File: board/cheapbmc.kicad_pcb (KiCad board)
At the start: 2 copper layers, 57.2 x 46.4 mm, 22 parts, among them J1 Conn_01x02_Male, J2 atxpanel, J3 atxpanel, J4 Conn_01x03_Male, K1 SILxx-1Axx-71x, K2 SILxx-1Axx-71x, Q1 BC547, Q2 BC547, SW1 SW_Push, U1 NodeMCU1.0(ESP-12E)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

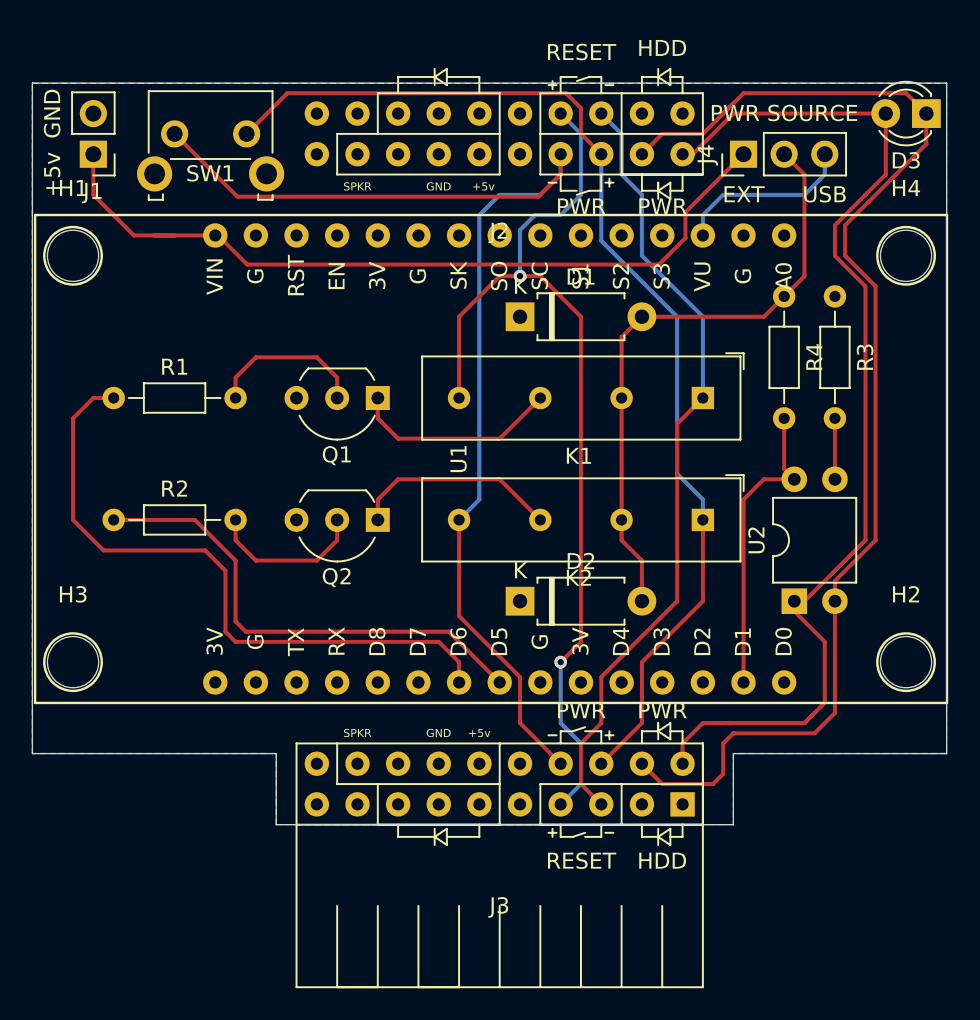
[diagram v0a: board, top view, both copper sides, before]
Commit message: remove text from mounting holes
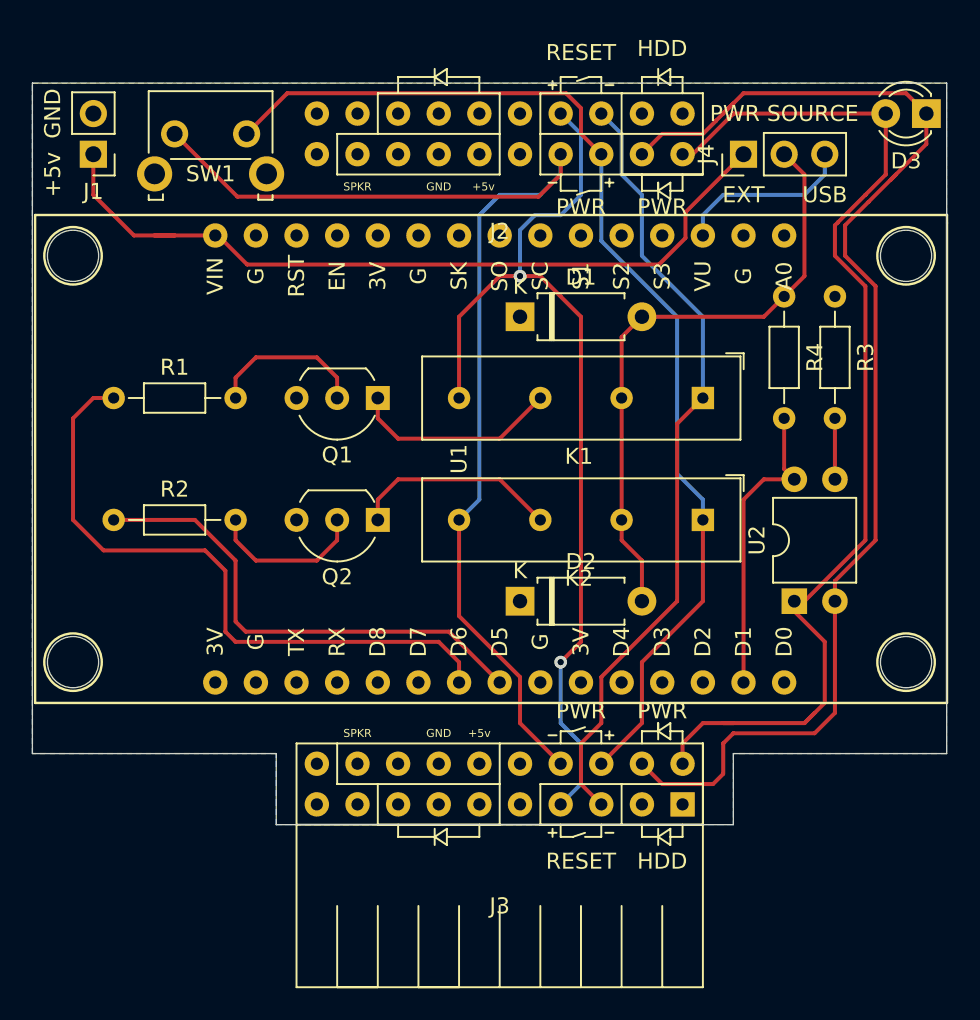
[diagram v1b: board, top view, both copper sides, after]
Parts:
-  : renamed from H4
-  : renamed from H3
-  : renamed from H2
-  : renamed from H1
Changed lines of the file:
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@@
     (tags "mounting hole 3.2mm no annular m3")
     (attr virtual)
-    (fp_text reference H4 (at 0 -4.2) (layer F.SilkS)
+    (fp_text reference " " (at 0 -4.2) (layer F.SilkS)
       (effects (font (size 1 1) (thickness 0.15)))
     )
@@
     (tags "mounting hole 3.2mm no annular m3")
     (attr virtual)
-    (fp_text reference H3 (at 0 -4.2) (layer F.SilkS)
+    (fp_text reference " " (at 0 -4.2) (layer F.SilkS)
       (effects (font (size 1 1) (thickness 0.15)))
     )
@@
     (tags "mounting hole 3.2mm no annular m3")
     (attr virtual)
-    (fp_text reference H2 (at 0 -4.2) (layer F.SilkS)
+    (fp_text reference " " (at 0 -4.2) (layer F.SilkS)
       (effects (font (size 1 1) (thickness 0.15)))
     )
@@
     (tags "mounting hole 3.2mm no annular m3")
     (attr virtual)
-    (fp_text reference H1 (at 0 -4.2) (layer F.SilkS)
+    (fp_text reference " " (at 0 -4.2) (layer F.SilkS)
       (effects (font (size 1 1) (thickness 0.15)))
     )

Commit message: board: Add current-limiting resistor on power status optoisolator
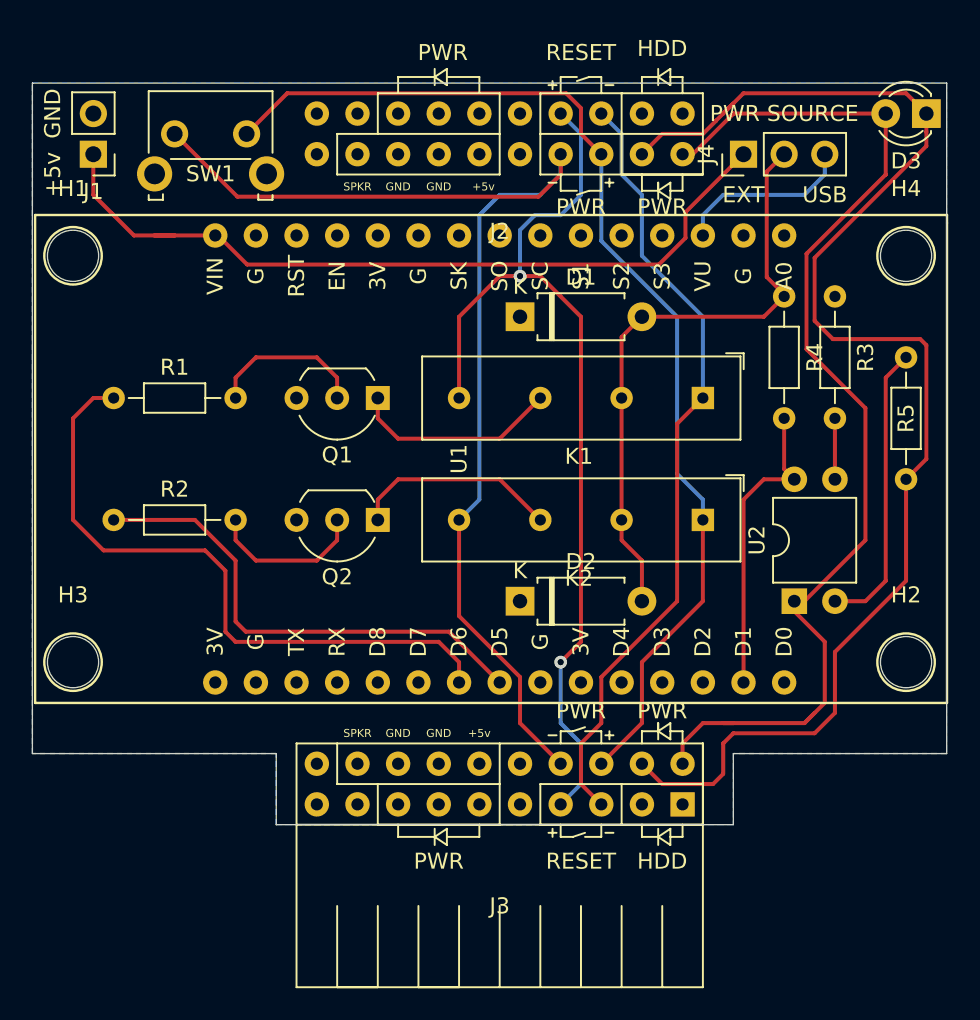
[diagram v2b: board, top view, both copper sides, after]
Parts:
- added R5: 220, Resistor_THT:R_Axial_DIN0204_L3.6mm_D1.6mm_P7.62mm_Horizontal, F.Cu at (163.8, 57.1)
- H1, H2, H3, H4: renamed from  
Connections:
- J2 pad 1: Net-(J2-Pad1) -> (no net)
- J2 pad 3: Net-(J2-Pad3) -> (no net)
- J3 pad 1: Net-(J3-Pad1) -> (no net)
- J3 pad 3: Net-(J3-Pad3) -> (no net)
- U1 pad 1: Net-(U1-Pad1) -> (no net)
- U1 pad 11: Net-(U1-Pad11) -> (no net)
- U1 pad 12: Net-(U1-Pad12) -> (no net)
- U1 pad 13: Net-(U1-Pad13) -> (no net)
- U1 pad 14: Net-(U1-Pad14) -> (no net)
- U1 pad 16: Net-(U1-Pad16) -> (no net)
- U1 pad 17: Net-(U1-Pad17) -> (no net)
- U1 pad 18: Net-(U1-Pad18) -> (no net)
- U1 pad 19: Net-(U1-Pad19) -> (no net)
- U1 pad 2: Net-(U1-Pad2) -> (no net)
- U1 pad 20: Net-(U1-Pad20) -> (no net)
- U1 pad 21: Net-(U1-Pad21) -> (no net)
- U1 pad 24: Net-(U1-Pad24) -> (no net)
- U1 pad 25: Net-(U1-Pad25) -> (no net)
- U1 pad 26: Net-(U1-Pad26) -> (no net)
- U1 pad 27: Net-(U1-Pad27) -> (no net)
- U1 pad 28: Net-(U1-Pad28) -> (no net)
- U1 pad 30: Net-(U1-Pad30) -> (no net)
- U1 pad 4: Net-(U1-Pad4) -> (no net)
- U1 pad 5: Net-(U1-Pad5) -> (no net)
- U1 pad 6: Net-(U1-Pad6) -> (no net)
- U1 pad 7: Net-(U1-Pad7) -> (no net)
- U1 pad 8: Net-(U1-Pad8) -> (no net)
- U1 pad 9: Net-(U1-Pad9) -> (no net)
- U2 pad 2: PWRLED_N -> Net-(R5-Pad1)
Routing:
- net Net-(R5-Pad1): track 0.00 -> 18.2 mm
- net PWRLED_N: track 78.2 -> 85.1 mm
- net PWRLED_P: track 70.0 -> 71.5 mm

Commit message: Move to kicad 6
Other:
- net class Default removed

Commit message: fix DRC, tidy up a bit
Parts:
- moved R4 1.27 mm to (156.2, 54.6)
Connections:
- J2 pad 1: (no net) -> unconnected-(J2-Pad1)
- J2 pad 3: (no net) -> unconnected-(J2-Pad3)
- J3 pad 1: (no net) -> unconnected-(J3-Pad1)
- J3 pad 3: (no net) -> unconnected-(J3-Pad3)
- U1 pad 1: (no net) -> unconnected-(U1-Pad1)
- U1 pad 11: (no net) -> unconnected-(U1-Pad11)
- U1 pad 12: (no net) -> unconnected-(U1-Pad12)
- U1 pad 13: (no net) -> unconnected-(U1-Pad13)
- U1 pad 14: (no net) -> unconnected-(U1-Pad14)
- U1 pad 16: (no net) -> unconnected-(U1-Pad16)
- U1 pad 17: (no net) -> unconnected-(U1-Pad17)
- U1 pad 18: (no net) -> unconnected-(U1-Pad18)
- U1 pad 19: (no net) -> unconnected-(U1-Pad19)
- U1 pad 2: (no net) -> unconnected-(U1-Pad2)
- U1 pad 20: (no net) -> unconnected-(U1-Pad20)
- U1 pad 21: (no net) -> unconnected-(U1-Pad21)
- U1 pad 24: (no net) -> unconnected-(U1-Pad24)
- U1 pad 25: (no net) -> unconnected-(U1-Pad25)
- U1 pad 26: (no net) -> unconnected-(U1-Pad26)
- U1 pad 27: (no net) -> unconnected-(U1-Pad27)
- U1 pad 28: (no net) -> unconnected-(U1-Pad28)
- U1 pad 30: (no net) -> unconnected-(U1-Pad30)
- U1 pad 4: (no net) -> unconnected-(U1-Pad4)
- U1 pad 5: (no net) -> unconnected-(U1-Pad5)
- U1 pad 6: (no net) -> unconnected-(U1-Pad6)
- U1 pad 7: (no net) -> unconnected-(U1-Pad7)
- U1 pad 8: (no net) -> unconnected-(U1-Pad8)
- U1 pad 9: (no net) -> unconnected-(U1-Pad9)
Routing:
- net PWRLED_P: track 71.5 -> 68.4 mm
- net Net-(J1-Pad1): track 50.2 -> 48.8 mm
- net PWRLED_TTL: track 19.2 -> 17.9 mm
- net PWRLED_N: track 85.1 -> 84.3 mm
